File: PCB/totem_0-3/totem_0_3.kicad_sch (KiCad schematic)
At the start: 88 parts, among them J1 MJ-4PP-9, J2 MJ-4PP-9, U1 xiao-ble, U2 xiao-ble

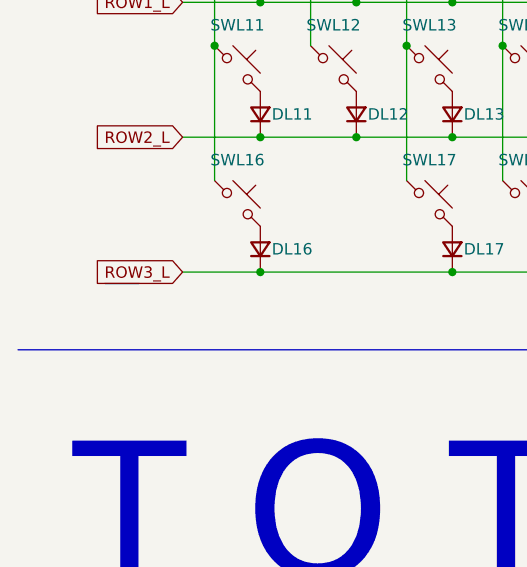
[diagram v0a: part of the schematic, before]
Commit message: initial tidyup and update to KiCad V8. Lots of footprints tweaked for PTH vs SMD, remove paste on lone parts to enable diode main area to have a stencil, add some more footprints to the project footprint library, start radiusing edges and increasing silk font size to suit JLC rules.
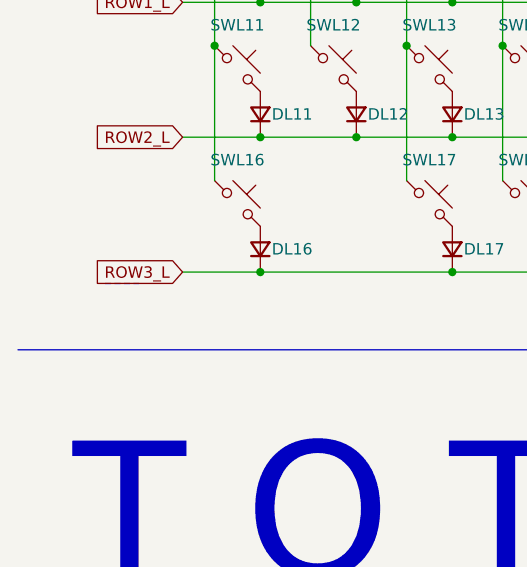
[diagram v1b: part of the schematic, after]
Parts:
- DL16, DR16: footprint TOTEMlib:Diode_SOD123 -> TOTEMlib:Diode_SOD123_noPaste
- PSW1, PSW2: footprint TOTEMlib:MSK12C02 -> TOTEMlib:MSK12C02_noPaste
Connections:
- net GND_L: now also RSW1.3 (MP)
- net GND_R: now also RSW2.MP
- net RESET_L: now also RSW1.MP
- net RESET_R: now also RSW2.MP
